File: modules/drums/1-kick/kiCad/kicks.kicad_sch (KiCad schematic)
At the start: 144 parts, among them J1 INPUT, J2 OUTPUT, J3 PWR, J4 INPUT, J5 INPUT, J6 OUTPUT, J7 INPUT, J8 INPUT, J9 INPUT, Q1 BC558, Q10 BC548, Q2 BC548, Q3 BC558, Q4 BC548, Q5 BC548, Q6 BC548, Q7 BC548, Q8 BC558, Q9 BC558, U1 TL074, U2 TL074, U3 TL074

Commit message: dd some more modules, update src for midi-2-cv
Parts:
- removed C10, C11, C12: 15nF, Synth:C_RECT_WIMA_0.1uF, symbol synth:C_sm (MKS)
- removed C13: 3.3nF, Synth:C_RECT_WIMA_0.1uF, symbol synth:C_sm (MKS)
- removed C7: 10nF, Synth:C_RECT_WIMA_0.1uF, symbol synth:C_sm (MKS)
- removed C8: 330nF, Synth:C_RECT_WIMA_0.1uF, symbol synth:C_sm (MKS)
- removed C9: 5.6nF, Synth:C_RECT_WIMA_0.1uF, symbol synth:C_sm (MKS)
- removed D10, D12, D4, D6, D7, D8, D9: 1N4148, Synth:D_DO-35_SOD27_P7.62mm_Horizontal, symbol synth:D_Signal (1N4148)
- removed D3: LED, Synth:LED_D5.0mm (center Aligned), symbol synth:LED (5mm)
- removed H1: H1, Synth:PinHeader_1x04_P2.54mm_Vertical, symbol synth:PinHeader_01x04
- removed H10, H11, H12, H13, H14, H15, H16, H9: MountingHole, MountingHole:MountingHole_3.2mm_M3, symbol Mechanical:MountingHole
- removed H17: H17, Synth:PinHeader_1x08_P2.54mm_Vertical, symbol synth:PinHeader_01x08
- removed H18: H18, Synth:PinSocket_1x08_P2.54mm_Vertical, symbol synth:PinSocket_01x08
- removed H2: H3, Synth:PinSocket_1x04_P2.54mm_Vertical, symbol synth:PinSocket_01x04
- removed H3: H5, Synth:PinHeader_1x04_P2.54mm_Vertical, symbol synth:PinHeader_01x04
- removed H4: H6, Synth:PinSocket_1x04_P2.54mm_Vertical, symbol synth:PinSocket_01x04
- removed H5: H7, Synth:PinHeader_1x04_P2.54mm_Vertical, symbol synth:PinHeader_01x04
- removed H6: H8, Synth:PinSocket_1x04_P2.54mm_Vertical, symbol synth:PinSocket_01x04
- removed H7: H2, Synth:PinHeader_1x08_P2.54mm_Vertical, symbol synth:PinHeader_01x08
- removed H8: H4, Synth:PinSocket_1x08_P2.54mm_Vertical, symbol synth:PinSocket_01x08
- removed J1, J4, J5, J9: INPUT, Synth:Jack_3.5mm_QingPu_WQP-PJ398SM_Vertical_CircularHoles, symbol synth:AudioJack_Mono_3.5mm
- removed J3: PWR, Synth:IDC-Header_2x08_P2.54mm_Vertical, symbol synth:Conn_02x08_EuroRack_Power
- removed Q1, Q3, Q9: BC558, Package_TO_SOT_THT:TO-92_Inline, symbol Transistor_BJT:BC558
- removed Q2, Q4, Q5: BC548, Package_TO_SOT_THT:TO-92_Inline, symbol Transistor_BJT:BC548
- removed R11: 122K, Synth:R_Default (DIN0207), symbol synth:R_Default
- removed R12, R16, R6, R8: 100K, Synth:R_Default (DIN0207), symbol synth:R_Default
- removed R13: 14K, Synth:R_Default (DIN0207), symbol synth:R_Default
- removed R14, R19: 10K, Synth:R_Default (DIN0207), symbol synth:R_Default
- removed R15, R22: 1K, Synth:R_Default (DIN0207), symbol synth:R_Default
- removed R17, R20: 1M, Synth:R_Default (DIN0207), symbol synth:R_Default
- removed R18: 2K, Synth:R_Default (DIN0207), symbol synth:R_Default
- removed R21, R4: 33K, Synth:R_Default (DIN0207), symbol synth:R_Default
- removed R23, R25: 47K, Synth:R_Default (DIN0207), symbol synth:R_Default
- removed R3: 680R, Synth:R_Default (DIN0207), symbol synth:R_Default
- removed R41, R9: 22K, Synth:R_Default (DIN0207), symbol synth:R_Default
- removed RV1, RV2: B100K, Synth:Potentiometer_TT_P0915N, symbol synth:R_Potentiometer (P0915N)
- removed RV4: B250K, Synth:Potentiometer_TT_P0915N, symbol synth:R_Potentiometer (P0915N)
- removed RV5: B50K, Synth:Potentiometer_TT_P0915N, symbol synth:R_Potentiometer (P0915N)
- removed RV6: A100K, Synth:Potentiometer_TT_P0915N, symbol synth:R_Potentiometer (P0915N)
- removed RV7: B1M, Synth:Potentiometer_TT_P0915N, symbol synth:R_Potentiometer (P0915N)
- removed TP10: DEPTH/PITCH, Connector_Pin:Pin_D1.0mm_L10.0mm, symbol Connector:TestPoint
- removed TP11: TONE, Connector_Pin:Pin_D1.0mm_L10.0mm, symbol Connector:TestPoint
- removed TP12: OUT, Connector_Pin:Pin_D1.0mm_L10.0mm, symbol Connector:TestPoint
- removed TP13: FINAL_IN, Connector_Pin:Pin_D1.0mm_L10.0mm, symbol Connector:TestPoint
- removed TP14: TONE_IN, Connector_Pin:Pin_D1.0mm_L10.0mm, symbol Connector:TestPoint
- removed TP15: TRIG_ACC, Connector_Pin:Pin_D1.0mm_L10.0mm, symbol Connector:TestPoint
- removed TP16: Q4_OUT, Connector_Pin:Pin_D1.0mm_L10.0mm, symbol Connector:TestPoint
- removed TP17: FEEDBACK, Connector_Pin:Pin_D1.0mm_L10.0mm, symbol Connector:TestPoint
- removed TP4: TRIG_IN, Connector_Pin:Pin_D1.0mm_L10.0mm, symbol Connector:TestPoint
- removed TP6: CV_IN, Connector_Pin:Pin_D1.0mm_L10.0mm, symbol Connector:TestPoint
- removed TP7: TRIG, Connector_Pin:Pin_D1.0mm_L10.0mm, symbol Connector:TestPoint
- removed TP8: DECAY_OUT, Connector_Pin:Pin_D1.0mm_L10.0mm, symbol Connector:TestPoint
- removed TP9: DECAY_IN, Connector_Pin:Pin_D1.0mm_L10.0mm, symbol Connector:TestPoint
- removed unit 2 of U1
- removed unit 1 of U1
- removed unit 3 of U1
- added D2: 1N4148, Diode_SMD:D_SOD-323_HandSoldering, symbol synth:D_Signal (1N4148)
- added D9: LED, Synth:LED_D3.0mm, symbol synth:LED (3mm)
- added H1: Conn_02x05_PWR_Eurorack, Synth:IDC-Header_2x05_P2.54mm_Vertical, symbol synth:Conn_02x05_EuroRack_Power
- added Q1: BC858, Package_TO_SOT_SMD:SOT-23, symbol Transistor_BJT:BC858
- added R1: 100K, Resistor_SMD:R_0805_2012Metric_Pad1.20x1.40mm_HandSolder, symbol synth:R_Default
- C1: renamed from C16; footprint Synth:C_RECT_WIMA_0.1uF -> Capacitor_SMD:C_0805_2012Metric_Pad1.18x1.45mm_HandSolder
- C10: renamed from C14; footprint Synth:C_RECT_WIMA_0.1uF -> Capacitor_SMD:C_0805_2012Metric_Pad1.18x1.45mm_HandSolder
- C11: renamed from C15; footprint Synth:C_RECT_WIMA_0.1uF -> Capacitor_SMD:C_0805_2012Metric_Pad1.18x1.45mm_HandSolder
- C2: renamed from C5; footprint Capacitor_THT:C_Rect_L4.6mm_W2.0mm_P2.50mm_MKS02_FKP02 -> Capacitor_SMD:C_0805_2012Metric_Pad1.18x1.45mm_HandSolder
- C3: renamed from C6; footprint Capacitor_THT:C_Rect_L4.6mm_W2.0mm_P2.50mm_MKS02_FKP02 -> Capacitor_SMD:C_0805_2012Metric_Pad1.18x1.45mm_HandSolder
- C4: renamed from C17; footprint Synth:C_RECT_WIMA_0.1uF -> Capacitor_SMD:C_0805_2012Metric_Pad1.18x1.45mm_HandSolder
- C5: renamed from C18; footprint Synth:C_RECT_WIMA_0.1uF -> Capacitor_SMD:C_0805_2012Metric_Pad1.18x1.45mm_HandSolder
- D1: renamed from D11; footprint Synth:D_DO-35_SOD27_P7.62mm_Horizontal -> Diode_SMD:D_SOD-323_HandSoldering
- D3: renamed from D13; footprint Synth:D_DO-35_SOD27_P7.62mm_Horizontal -> Diode_SMD:D_SOD-323_HandSoldering
- D5: footprint Synth:D_DO-35_SOD27_P7.62mm_Horizontal -> Diode_SMD:D_SOD-323_HandSoldering
- D6: renamed from D1; footprint Synth:D_DO-41_SOD81_P10.16mm_Horizontal -> Diode_SMD:D_SOD-123
- D7: renamed from D2; footprint Synth:D_DO-41_SOD81_P10.16mm_Horizontal -> Diode_SMD:D_SOD-123
- D8: renamed from D14; footprint Synth:D_DO-35_SOD27_P7.62mm_Horizontal -> Diode_SMD:D_SOD-323_HandSoldering
- J2: value OUTPUT -> INPUT
- Q2: renamed from Q10; value BC548 -> BC848; footprint Package_TO_SOT_THT:TO-92_Inline -> Package_TO_SOT_SMD:SOT-23; symbol Transistor_BJT:BC548 -> Transistor_BJT:BC848
- Q3: renamed from Q8; value BC558 -> BC858; footprint Package_TO_SOT_THT:TO-92_Inline -> Package_TO_SOT_SMD:SOT-23; symbol Transistor_BJT:BC558 -> Transistor_BJT:BC858
- Q4: renamed from Q7; value BC548 -> BC848; footprint Package_TO_SOT_THT:TO-92_Inline -> Package_TO_SOT_SMD:SOT-23; symbol Transistor_BJT:BC548 -> Transistor_BJT:BC848
- Q5: renamed from Q6; value BC548 -> BC848; footprint Package_TO_SOT_THT:TO-92_Inline -> Package_TO_SOT_SMD:SOT-23; symbol Transistor_BJT:BC548 -> Transistor_BJT:BC848
- R10: footprint Synth:R_Default (DIN0207) -> Resistor_SMD:R_0805_2012Metric_Pad1.20x1.40mm_HandSolder
- R11: renamed from R1; footprint Synth:R_Default (DIN0207) -> Resistor_SMD:R_0805_2012Metric_Pad1.20x1.40mm_HandSolder
- R12: renamed from R2; footprint Synth:R_Default (DIN0207) -> Resistor_SMD:R_0805_2012Metric_Pad1.20x1.40mm_HandSolder
- R13: renamed from R37; footprint Synth:R_Default (DIN0207) -> Resistor_SMD:R_0805_2012Metric_Pad1.20x1.40mm_HandSolder
- R14: renamed from R39; footprint Synth:R_Default (DIN0207) -> Resistor_SMD:R_0805_2012Metric_Pad1.20x1.40mm_HandSolder
- R15: renamed from R28; footprint Synth:R_Default (DIN0207) -> Resistor_SMD:R_0805_2012Metric_Pad1.20x1.40mm_HandSolder
- R16: renamed from R40; footprint Synth:R_Default (DIN0207) -> Resistor_SMD:R_0805_2012Metric_Pad1.20x1.40mm_HandSolder
- R17: renamed from R33; footprint Synth:R_Default (DIN0207) -> Resistor_SMD:R_0805_2012Metric_Pad1.20x1.40mm_HandSolder
- R18: renamed from R32; footprint Synth:R_Default (DIN0207) -> Resistor_SMD:R_0805_2012Metric_Pad1.20x1.40mm_HandSolder
- R19: renamed from R27; footprint Synth:R_Default (DIN0207) -> Resistor_SMD:R_0805_2012Metric_Pad1.20x1.40mm_HandSolder
- R2: renamed from R29; value 47K -> 39K; footprint Synth:R_Default (DIN0207) -> Resistor_SMD:R_0805_2012Metric_Pad1.20x1.40mm_HandSolder
- R20: renamed from R34; footprint Synth:R_Default (DIN0207) -> Resistor_SMD:R_0805_2012Metric_Pad1.20x1.40mm_HandSolder
- R21: renamed from R35; footprint Synth:R_Default (DIN0207) -> Resistor_SMD:R_0805_2012Metric_Pad1.20x1.40mm_HandSolder
- R22: renamed from R36; footprint Synth:R_Default (DIN0207) -> Resistor_SMD:R_0805_2012Metric_Pad1.20x1.40mm_HandSolder
- R23: renamed from R26; footprint Synth:R_Default (DIN0207) -> Resistor_SMD:R_0805_2012Metric_Pad1.20x1.40mm_HandSolder
- R24: value 470R -> 1K; footprint Synth:R_Default (DIN0207) -> Resistor_SMD:R_0805_2012Metric_Pad1.20x1.40mm_HandSolder
- R3: renamed from R30; footprint Synth:R_Default (DIN0207) -> Resistor_SMD:R_0805_2012Metric_Pad1.20x1.40mm_HandSolder
- R4: renamed from R31; footprint Synth:R_Default (DIN0207) -> Resistor_SMD:R_0805_2012Metric_Pad1.20x1.40mm_HandSolder
- R5: value 100K -> 1K; footprint Synth:R_Default (DIN0207) -> Resistor_SMD:R_0805_2012Metric_Pad1.20x1.40mm_HandSolder
- R6: renamed from R42; footprint Synth:R_Default (DIN0207) -> Resistor_SMD:R_0805_2012Metric_Pad1.20x1.40mm_HandSolder
- R7: value 47K -> 22K; footprint Synth:R_Default (DIN0207) -> Resistor_SMD:R_0805_2012Metric_Pad1.20x1.40mm_HandSolder
- R8: renamed from R43; footprint Synth:R_Default (DIN0207) -> Resistor_SMD:R_0805_2012Metric_Pad1.20x1.40mm_HandSolder
- R9: renamed from R38; footprint Synth:R_Default (DIN0207) -> Resistor_SMD:R_0805_2012Metric_Pad1.20x1.40mm_HandSolder
- RV4: renamed from RV8; value B100K -> B250K
- TP5: value ACC_IN -> RES
- U1: footprint Package_DIP:DIP-14_W7.62mm_Socket_LongPads -> Package_SO:SO-14_3.9x8.65mm_P1.27mm
- U1: renamed from U2; footprint Package_DIP:DIP-14_W7.62mm_Socket_LongPads -> Package_SO:SO-14_3.9x8.65mm_P1.27mm
- U1: renamed from U3; footprint Package_DIP:DIP-14_W7.62mm_Socket_LongPads -> Package_SO:SO-14_3.9x8.65mm_P1.27mm
- renumbered C1 to C6, C2 to C7, C3 to C8, C4 to C9, J7 to J1, J8 to J3, J6 to J4, RV10 to RV1, RV11 to RV2, RV9 to RV5, TP18 to TP1, TP1 to TP2, TP2 to TP3, TP3 to TP4
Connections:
- net +12V: now also Q2.3 (C), Q4.3 (C); no longer Q2.1 (C), Q4.1 (C), R5.2
- net GNDREF: now also J4.TN, Q3.3 (C), R24.2, RV3.3, U1.10 (+), D2.2 (A), H1.3 (Pin_3), H1.4 (Pin_4), H1.5 (Pin_5), H1.6 (Pin_6), H1.7 (Pin_7), H1.8 (Pin_8), Q1.3 (C), R1.2; no longer Q3.1 (C), R16.1, R7.2, RV3.1, U1.5 (+)
- net at U1.13 (-): now also R24.1, D9.1 (K)
- net at U1.14: now also D9.2 (A)
- net at U1.12 (+): now also C11.2, R17.2, R20.1, R23.1, U1.7
- net at C1.1, J1.T: now also R1.1
- net at C1.2, D1.1 (K), R2.1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: now also U1.3 (+); no longer U1.10 (+)
- net at R6.1, R8.2: now also Q2.1 (B), R7.1; no longer Q2.2 (B)
- net at D3.2 (A): now also Q2.2 (E), R15.2; no longer Q2.3 (E)
- net at C5.1, R13.1: now also Q4.2 (E); no longer Q4.3 (E)
- net at C10.2, C11.1, R14.2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: now also Q5.3 (C); no longer Q5.1 (C)
- net at D7.1 (K): now also H1.1 (Pin_1), H1.2 (Pin_2)
- net at C4.2, D3.1 (K), RV1.1: now also Q4.1 (B); no longer Q4.2 (B)
- net at R21.2, R22.2, RV5.3: now also TP5.1, U1.8; no longer U1.7
- net at R13.2: now also Q5.1 (B); no longer Q5.2 (B)
- net at R16.2: now also Q5.2 (E); no longer Q5.3 (E)
- net at D6.2 (A): now also H1.10 (Pin_10), H1.9 (Pin_9)
- net at R3.1, R4.2: now also U1.2 (-); no longer U1.9 (-)
- net at J2.T: now also R5.2
- net at RV3.2: now also R16.1, RV3.1; no longer RV3.3
- net at R10.2: now also J3.T
- net at R9.1: now also Q3.2 (E); no longer Q3.3 (E)
- net at RV2.2: now also D5.1 (K), Q3.1 (B); no longer Q3.2 (B)
- net at R6.2: now also U1.1; no longer U1.8
- net at RV2.1: now also R10.1; no longer J3.T
- net at R20.2, R22.1, RV5.1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: now also U1.9 (-); no longer U1.6 (-)
- net at R5.1: now also D2.1 (K), Q1.1 (B)
- new net: Q1.2 (E), R7.2
- no-connect marks 14 -> 4
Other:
- note added: "Accent"
- note added: "Decay"
- note added: "Pitch"
- note added: "Pitch CV"
- note added: "Trigger"
- note added: "Tune Decay"
- note added: "Tune Depth"
- note added: "Why?"
- note removed: "CV PITCH"
- note removed: "DECAY"
- note removed: "DEPTH"
- note removed: "DISTORT"
- note removed: "PITCH"
- note removed: "TONE"
- note removed: "TONE DECAY"
- note removed: "UNTESTED"
- moved on the sheet: C1, C10, C11, C2, C3, C4, C5, C6, C7, C8, C9, D1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

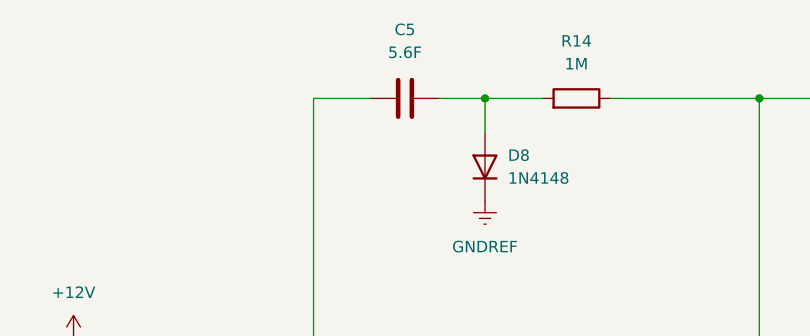
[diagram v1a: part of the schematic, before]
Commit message: debugging and rework for ricochet, midas, wolkje. Added IBOM for drums and other modules.
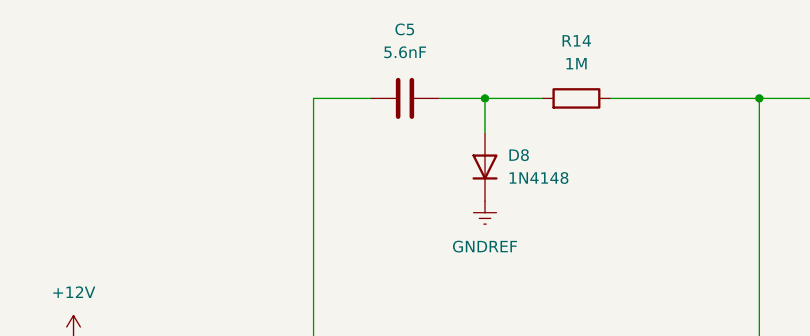
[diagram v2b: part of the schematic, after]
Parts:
- C5: value 5.6F -> 5.6nF
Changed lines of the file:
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@@
 			)
 		)
-		(property "Value" "5.6F"
+		(property "Value" "5.6nF"
 			(at 255.27 53.34 90)
 			(effects

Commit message: quantizers_stls
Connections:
- net GNDREF: now also J4.S; no longer J4.TN
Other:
- note added: "Rev.1: Output footprint is wrongly connected to ground, sleeve is floating (J4)"
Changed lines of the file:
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@@
 (kicad_sch
-	(version 20231120)
+	(version 20250114)
 	(generator "eeschema")
-	(generator_version "8.0")
+	(generator_version "9.0")
 	(paper "A3")
+	(rectangle
+		(start 172.72 251.46)
+		(end 190.5 284.48)
+		(stroke
+			(width 0.254)
+			(type dot)
+		)
+		(fill
+			(type none)
+		)
+	)
+	(rectangle
+		(start 193.04 243.84)
+		(end 294.64 284.48)
+		(stroke
+			(width 0.25)
+			(type dot)
+		)
+		(fill
+			(type none)
+		)
+	)
+	(rectangle
+		(start 137.16 251.46)
+		(end 170.18 284.48)
+		(stroke
+			(width 0.25)
+			(type dot)
+		)
+		(fill
+			(type none)
+		)
+	)
+	(text "Rev.1: Output footprint is wrongly connected to ground, sleeve is floating (J4)\n"
+		(exclude_from_sim no)
+		(at 300.736 255.27 0)
+		(effects
+			(font
+				(size 1.27 1.27)
+			)
+			(justify left)
+		)
+	)
+	(text "Trigger"
+		(exclude_from_sim no)
+		(at 29.21 164.084 0)
+		(effects
+			(font
+				(size 1.27 1.27)
+			)
+		)
+	)
+	(text "Pitch"
+		(exclude_from_sim no)
+		(at 299.466 112.268 0)
+		(effects
+			(font
+				(size 1.27 1.27)
+			)
+		)
+	)
+	(text "Decay"
+		(exclude_from_sim no)
+		(at 363.22 81.28 0)
+		(effects
+			(font
+				(size 1.27 1.27)
+			)
+		)
+	)
+	(text "Tune\nDepth"
+		(exclude_from_sim no)
+		(at 289.814 134.62 0)
+		(effects
+			(font
+				(size 1.27 1.27)
+			)
+		)
+	)
+	(text "Why?"
+		(exclude_from_sim no)
+		(at 41.91 187.96 0)
+		(effects
+			(font
+				(size 1.27 1.27)
+			)
+		)
+	)
+	(text "Tune Decay"
+		(exclude_from_sim no)
+		(at 203.708 97.028 0)
+		(effects
+			(font
+				(size 1.27 1.27)
+			)
+		)
+	)
+	(text "Accent"
+		(exclude_from_sim no)
+		(at 77.216 151.384 0)
+		(effects
+			(font
+				(size 1.27 1.27)
+			)
+		)
+	)
+	(text "Lennart Querter"
+		(exclude_from_sim no)
+		(at 399.542 267.208 0)
+		(effects
+			(font
+				(size 1.27 1.27)
+			)
+		)
+	)
+	(text "1"
+		(exclude_from_sim no)
+		(at 391.922 280.67 0)
+		(effects
+			(font
+				(size 1.27 1.27)
+			)
+		)
+	)
+	(text "Pitch CV"
+		(exclude_from_sim no)
+		(at 239.268 137.922 0)
+		(effects
+			(font
+				(size 1.27 1.27)
+			)
+		)
+	)
 	(junction
 		(at 196.85 107.95)
@@
 	)
 	(no_connect
-		(at 392.43 179.07)
+		(at 31.75 179.07)
 	)
 	(no_connect
-		(at 31.75 179.07)
+		(at 392.43 173.99)
 	)
 	(no_connect
@@
 		)
 	)
-	(rectangle
-		(start 172.72 251.46)
-		(end 190.5 284.48)
-		(stroke
-			(width 0.254)
-			(type dot)
-		)
-		(fill
-			(type none)
-		)
-	)
-	(rectangle
-		(start 193.04 243.84)
-		(end 294.64 284.48)
-		(stroke
-			(width 0.25)
-			(type dot)
-		)
-		(fill
-			(type none)
-		)
-	)
-	(rectangle
-		(start 137.16 251.46)
-		(end 170.18 284.48)
-		(stroke
-			(width 0.25)
-			(type dot)
-		)
-		(fill
-			(type none)
-		)
-	)
-	(text "Trigger"
-		(exclude_from_sim no)
-		(at 29.21 164.084 0)
-		(effects
-			(font
-				(size 1.27 1.27)
-			)
-		)
-	)
-	(text "Pitch"
-		(exclude_from_sim no)
-		(at 299.466 112.268 0)
-		(effects
-			(font
-				(size 1.27 1.27)
-			)
-		)
-	)
-	(text "Decay"
-		(exclude_from_sim no)
-		(at 363.22 81.28 0)
-		(effects
-			(font
-				(size 1.27 1.27)
-			)
-		)
-	)
-	(text "Tune\nDepth"
-		(exclude_from_sim no)
-		(at 289.814 134.62 0)
-		(effects
-			(font
-				(size 1.27 1.27)
-			)
-		)
-	)
-	(text "Why?"
-		(exclude_from_sim no)
-		(at 41.91 187.96 0)
-		(effects
-			(font
-				(size 1.27 1.27)
-			)
-		)
-	)
-	(text "Tune Decay"
-		(exclude_from_sim no)
-		(at 203.708 97.028 0)
-		(effects
-			(font
-				(size 1.27 1.27)
-			)
-		)
-	)
-	(text "Accent"
-		(exclude_from_sim no)
-		(at 77.216 151.384 0)
-		(effects
-			(font
-				(size 1.27 1.27)
-			)
-		)
-	)
-	(text "Lennart Querter"
-		(exclude_from_sim no)
-		(at 399.542 267.208 0)
-		(effects
-			(font
-				(size 1.27 1.27)
-			)
-		)
-	)
-	(text "1"
-		(exclude_from_sim no)
-		(at 391.922 280.67 0)
-		(effects
-			(font
-				(size 1.27 1.27)
-			)
-		)
-	)
-	(text "Pitch CV"
-		(exclude_from_sim no)
-		(at 239.268 137.922 0)
-		(effects
-			(font
-				(size 1.27 1.27)
-			)
-		)
-	)
 	(symbol
 		(lib_id "synth:R_Default")
@@
 					(size 1.27 1.27)
 				)
+				(hide yes)
 			)
 		)
@@
 					(size 1.27 1.27)
 				)
+				(hide yes)
 			)
 		)
@@
 					(size 1.27 1.27)
 				)
+				(hide yes)
 			)
 		)
@@
 					(size 1.27 1.27)
 				)
+				(hide yes)
 			)
 		)
@@
 					(size 1.27 1.27)
 				)
+				(hide yes)
 			)
 		)
@@
 				)
 				(justify right)
+				(hide yes)
 			)
 		)
@@
 					(size 1.27 1.27)
 				)
+				(hide yes)
 			)
 		)
@@
 					(size 1.27 1.27)
 				)
+				(hide yes)
 			)
 		)
@@
 				)
 				(justify left)
+				(hide yes)
 			)
 		)
@@
 					(size 1.27 1.27)
 				)
+				(hide yes)
 			)
 		)
@@
 					(size 1.27 1.27)
 				)
+				(hide yes)
 			)
 		)
@@
 					(size 1.27 1.27)
 				)
+				(hide yes)
 			)
 		)
@@
 	(symbol
 		(lib_id "power:GNDREF")
-		(at 392.43 173.99 270)
+		(at 392.43 179.07 0)
 		(unit 1)
 		(exclude_from_sim no)
@@
 		(fields_autoplaced yes)
 		(property "Reference" "#PWR035"
-			(at 386.08 173.99 0)
+			(at 392.43 185.42 0)
 			(effects
 				(font
@@
 		)
 		(property "Value" "GNDREF"
-			(at 388.62 173.9899 90)
+			(at 392.43 184.15 0)
 			(effects
 				(font
 					(size 1.27 1.27)
 				)
-				(justify right)
+				(hide yes)
 			)
 		)
 		(property "Footprint" ""
-			(at 392.43 173.99 0)
+			(at 392.43 179.07 0)
 			(effects
 				(font
@@
 		)
 		(property "Datasheet" ""
-			(at 392.43 173.99 0)
+			(at 392.43 179.07 0)
 			(effects
 				(font
@@
 		)
 		(property "Description" "Power symbol creates a global label with name \"GNDREF\" , reference supply ground"
-			(at 392.43 173.99 0)
+			(at 392.43 179.07 0)
 			(effects
 				(font
@@
 					(size 1.27 1.27)
 				)
+				(hide yes)
 			)
 		)
@@
 					(size 1.27 1.27)
 				)
+				(hide yes)
 			)
 		)
@@
 				)
 				(justify right)
+				(hide yes)
 			)
 		)
@@
 		)
 	)
+	(embedded_fonts no)
 )
